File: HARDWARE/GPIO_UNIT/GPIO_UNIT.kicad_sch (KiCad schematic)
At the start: 0 parts

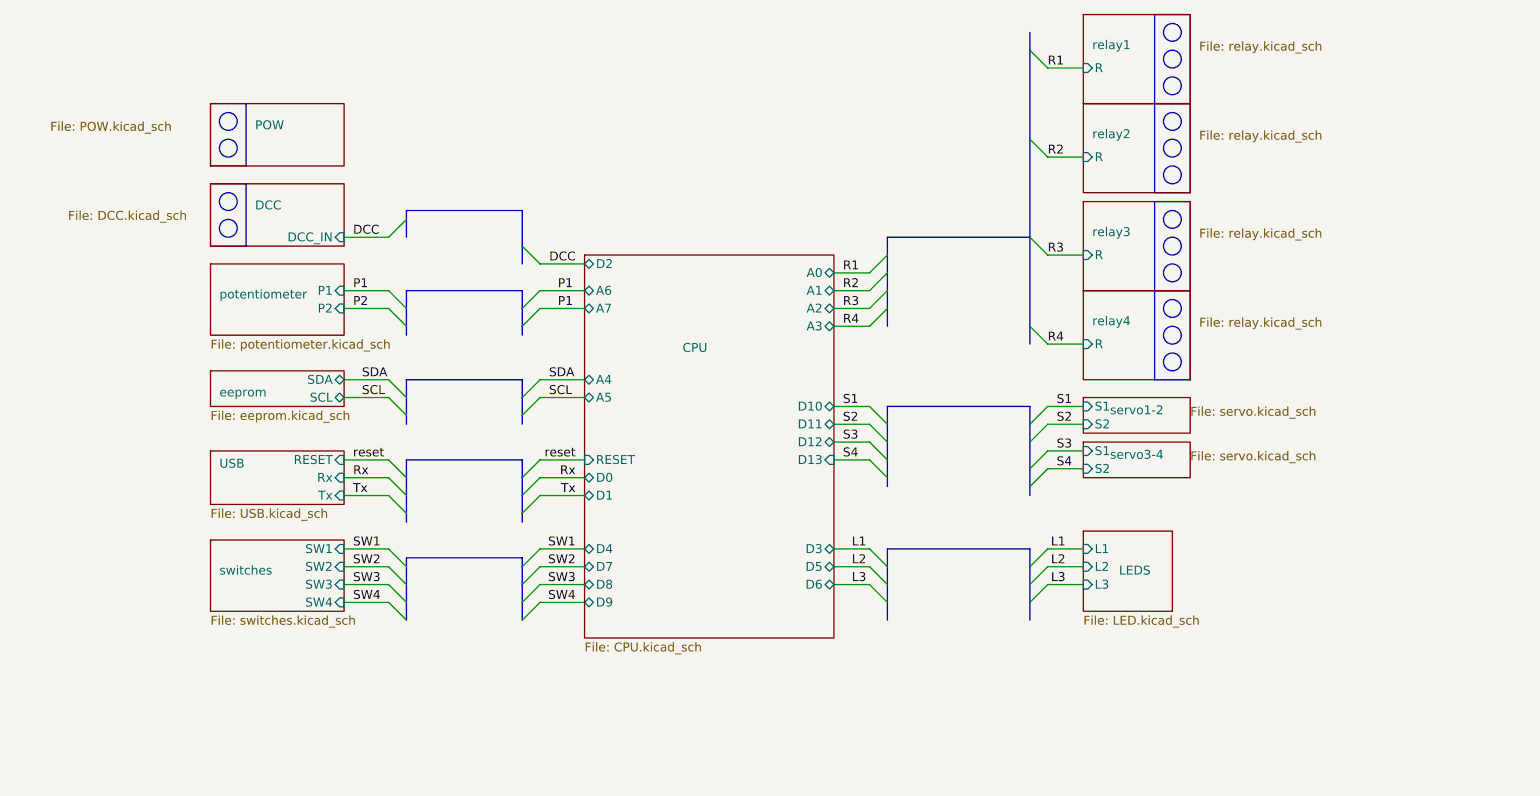
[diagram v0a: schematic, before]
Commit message: added GPIO UNIT board. To be renamed Jack Of All trades
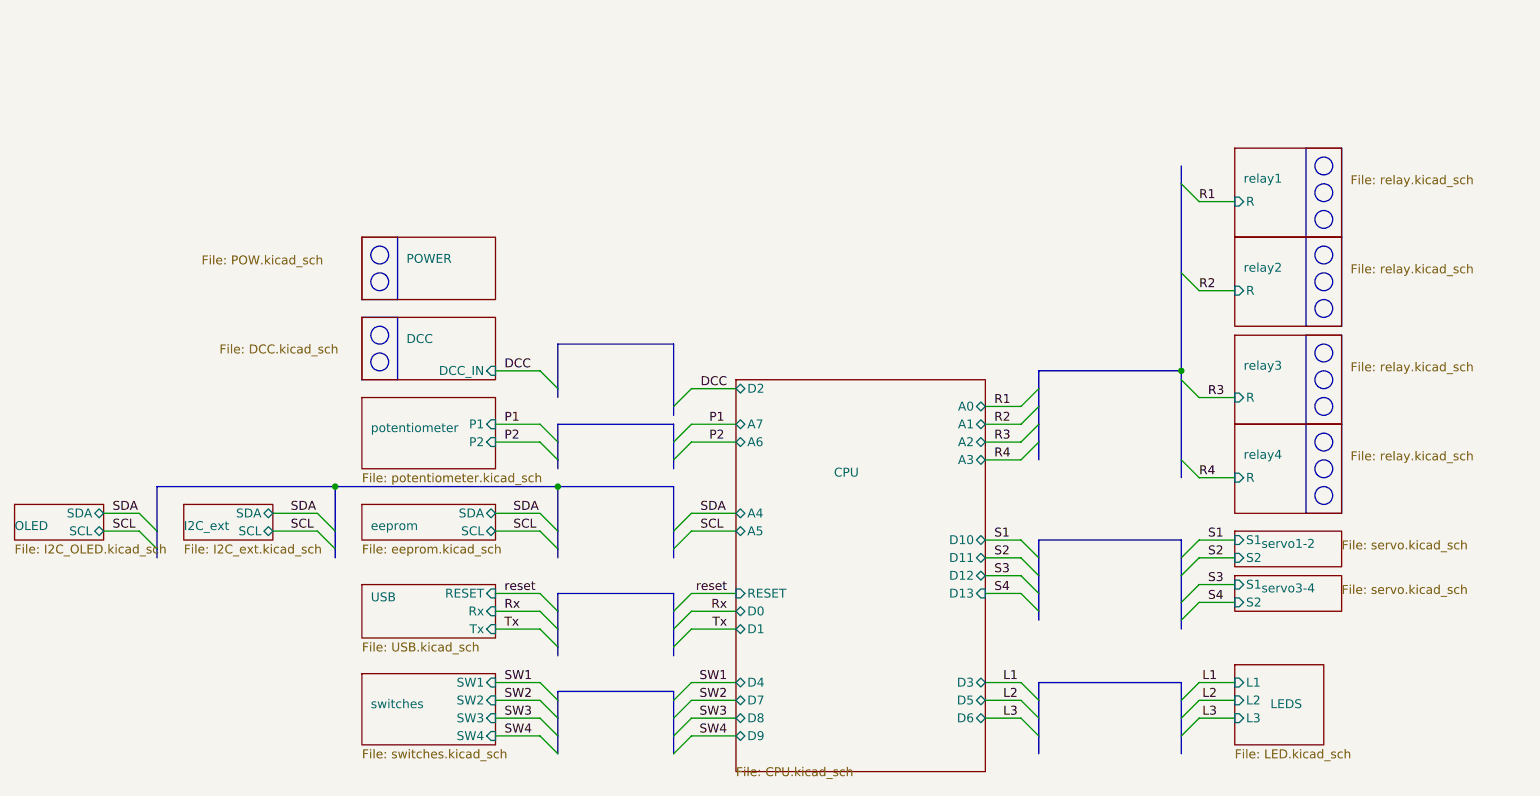
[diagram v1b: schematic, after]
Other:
- sheet POW renamed POWER
- added sheet I2C_ext (I2C_ext.kicad_sch)
- added sheet OLED (I2C_OLED.kicad_sch)
